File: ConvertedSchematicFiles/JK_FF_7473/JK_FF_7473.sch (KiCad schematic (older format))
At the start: 6 parts, among them U1 7473

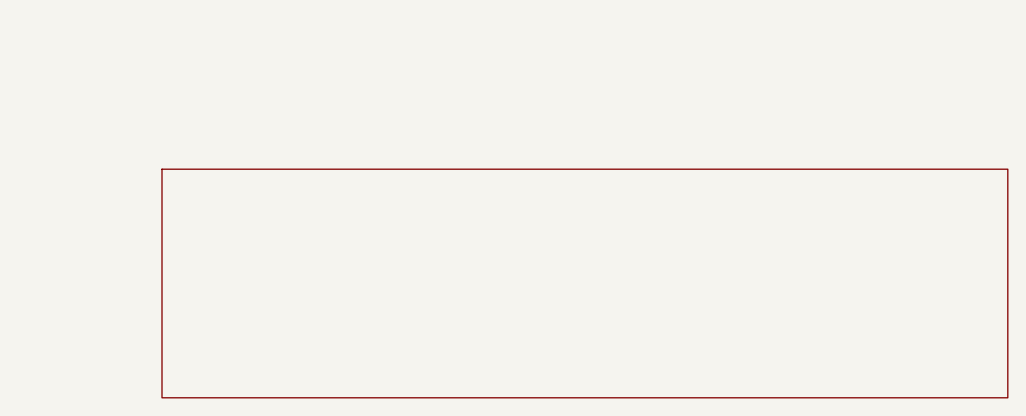
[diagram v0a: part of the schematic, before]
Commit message: Excluded some components. These no longer appear after conversion. When calling shell commands, filenames are in "quotes"
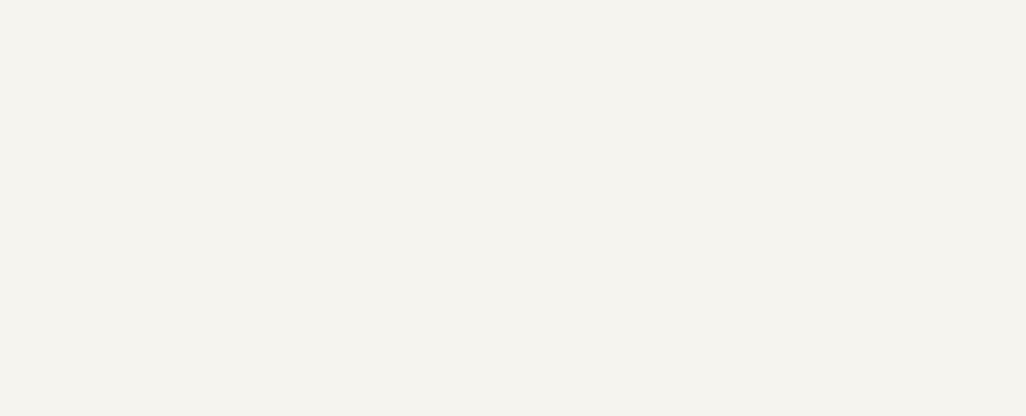
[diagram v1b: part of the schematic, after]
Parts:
- removed titleblk: titleblk, symbol TITLEBLK_PSPICE
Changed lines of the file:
@@
-	1    0    0    1
-$EndComp
-$Comp
-L TITLEBLK_PSPICE titleblk
-U 1 1 74238335
-P 11880 8400
-F 0 "titleblk" H 23760 16800 30  0001 L CNN
-F 1 "titleblk" H 23760 16880 30  0001 L CNN
-	1    11880 8400
 	1    0    0    1
 $EndComp

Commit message: Ports issue fixed. Now annotation for ports is #PWR? function added "itos"
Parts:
- removed EGND: EGND, symbol EGND_PSPICE
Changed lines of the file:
@@
 $EndDescr
 $Comp
-L EGND_PSPICE EGND
+L EGND_PSPICE #PWR1
 U 1 1 14289383
 P 2900 700
-F 0 "EGND" H 5800 1400 30  0001 L CNN
+F 0 "#PWR1" H 5800 1400 30  0001 L CNN
 F 1 "EGND" H 5800 1480 30  0001 L CNN
 	1    2900 700

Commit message: Added LICENSE.txt
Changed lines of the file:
@@
 $EndDescr
 $Comp
-L EGND_PSPICE #PWR1
+L GND #PWR1
 U 1 1 14289383
 P 2900 700

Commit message: Orientation fix. Library components are now inverted, with +ve y axis going up. In Schematic files, +ve y axis is downwards. This is how the KiCad libraries are. As a result of the above fixed, the converted GND is now oriented correctly.
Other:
- moved on the sheet: U1, V1
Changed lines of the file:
@@
 F 1 "EGND" H 5800 1480 30  0001 L CNN
 	1    2900 700
-	1    0    0    1
+	1    0    0    -1
 $EndComp
 $Comp
@@
 F 1 "DigClock" H 1500 1080 30  0000 L CNN
 	1    1500 1000
-	1    0    0    1
+	1    0    0    -1
 $EndComp
 $Comp
@@
 F 1 "5V" H 2900 190 30  0000 C CNN
 	1    2900 300
-	1    0    0    1
+	1    0    0    -1
 $EndComp
 $Comp
@@
 F 1 "DigStim" H 1500 1580 30  0000 L CNN
 	1    1500 1500
-	1    0    0    1
+	1    0    0    -1
 $EndComp
 $Comp
@@
 F 1 "7473" H 1900 880 30  0000 L CNN
 	1    1900 800
-	1    0    0    1
+	1    0    0    -1
 $EndComp
 Wire Wire Line

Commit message: Removed the use of exec, wrote basename function, made integration with eSim easier.
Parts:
- added titleblk: titleblk, symbol titleblk_PSPICE
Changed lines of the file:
@@
-EESchema Schematic File Version 2  date Saturday 17 July 1999 11:36:18 AM IST
+EESchema Schematic File Version 2  date
 LIBS:power
 LIBS:device
@@
 LIBS:contrib
 LIBS:valves
-LIBS:ConvertedSchematicFiles/JK_FF_7473-cache
 EELAYER 25  0
 EELAYER END
@@
 Sheet 1 1
 Title ""
-Date "17 Jul 1999"
+Date ""
 Rev ""
 Comp ""
@@
 	1    0    0    -1
 $EndComp
+$Comp
+L titleblk_PSPICE titleblk
+U 1 1 74238335
+P 11880 8400
+F 0 "titleblk" H 23760 16800 30  0001 L CNN
+F 1 "titleblk" H 23760 16880 30  0001 L CNN
+	1    11880 8400
+	1    0    0    -1
+$EndComp
